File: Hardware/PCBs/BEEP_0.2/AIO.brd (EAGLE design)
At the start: 106.2 x 69.1 mm, 85 parts, among them IC1 ULN2803ASOP18, IC2 ULN2803ASOP18, IC3 74HC238SSOP, IC4 74HC238SSOP, IC5 TS34119SMD, U2 TB6612FNG, U3 ATXMEGA64D3-AU, X1 MICROMATCH-4, X10 MICROMATCH-10, X3 MICROMATCH-8, X4 MICROMATCH-8, X5 MICROMATCH-8, X8 MICROMATCH-8, X9 MICROMATCH-4

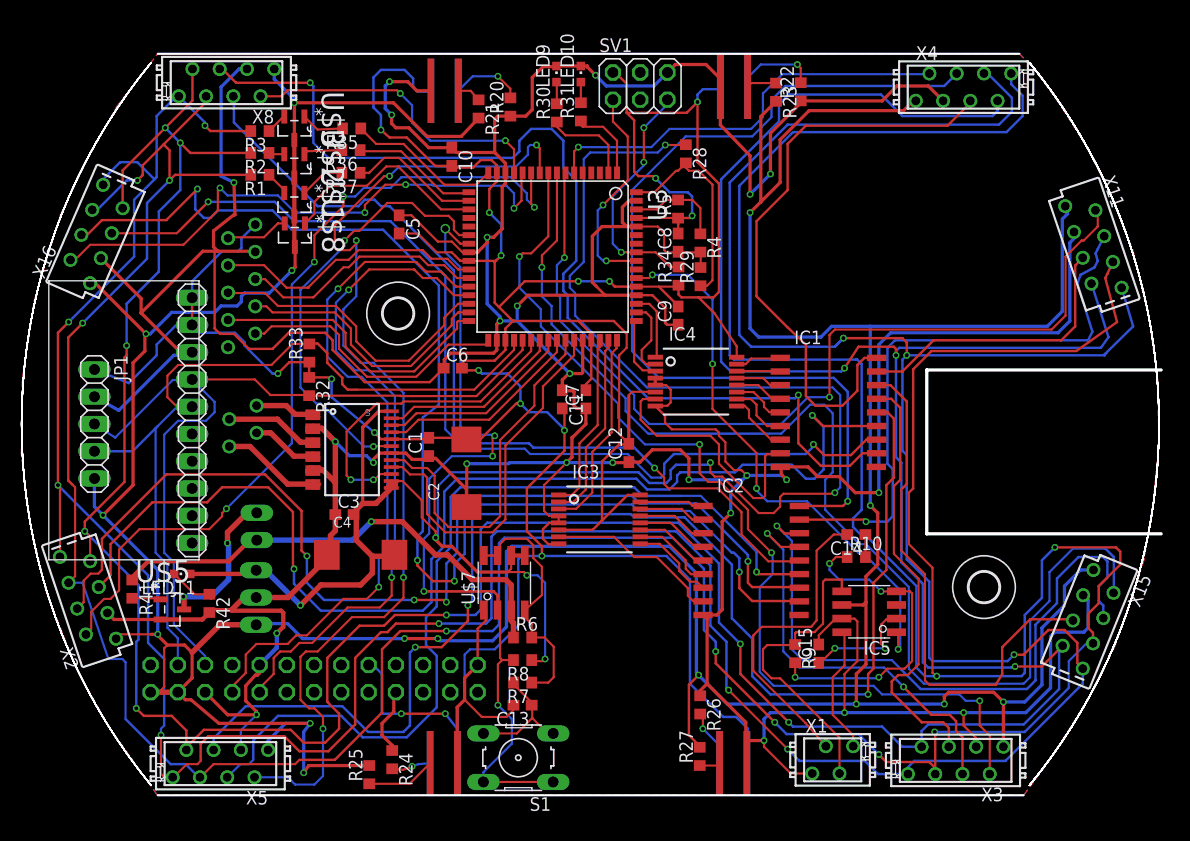
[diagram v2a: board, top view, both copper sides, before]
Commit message: rearrange connectors routing
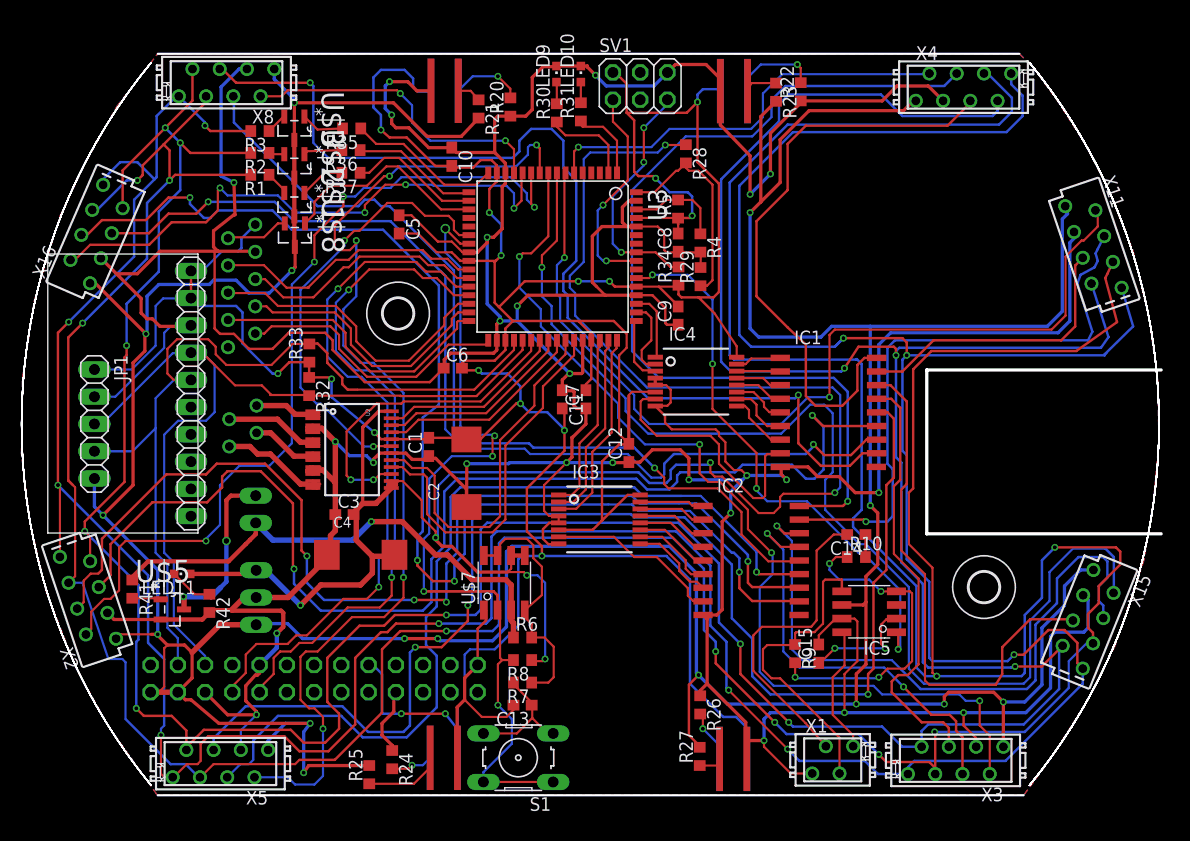
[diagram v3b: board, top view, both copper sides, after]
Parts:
- moved U$25 2.50 mm to (6.25, 43.1)
- moved JP13 1.60 mm to (18.6, 32.4)
- moved U$23 0.50 mm to (36.2, 12.2)
- moved U$22 0.40 mm to (63.2, 68.3)
- moved U$24 0.40 mm to (63.1, 12.1)
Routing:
- net SCL: track 78.5 -> 82.8 mm
- net SDA: track 77.5 -> 81.1 mm
- net +5V: track 397.0 -> 399.7 mm
- net LED_K5_OUT: track 106.6 -> 108.9 mm
- net BATT_GND: track 14.0 -> 16.3 mm
- net ADISTANCE_5: track 78.3 -> 80.5 mm
- net BATT_U: track 45.2 -> 47.1 mm
- net +3V3: track 368.6 -> 370.4 mm
- net IR_LED_K6_OUT: track 115.8 -> 114.1 mm
- net IR_LED_K5_OUT: track 98.0 -> 99.4 mm
- net N$20: track 6.48 -> 7.22 mm
- net GND: track 617.5 -> 618.2 mm

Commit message: move folders try to apply drc from sparkfun (wip) moved audio connetor add slice for camera flexcable
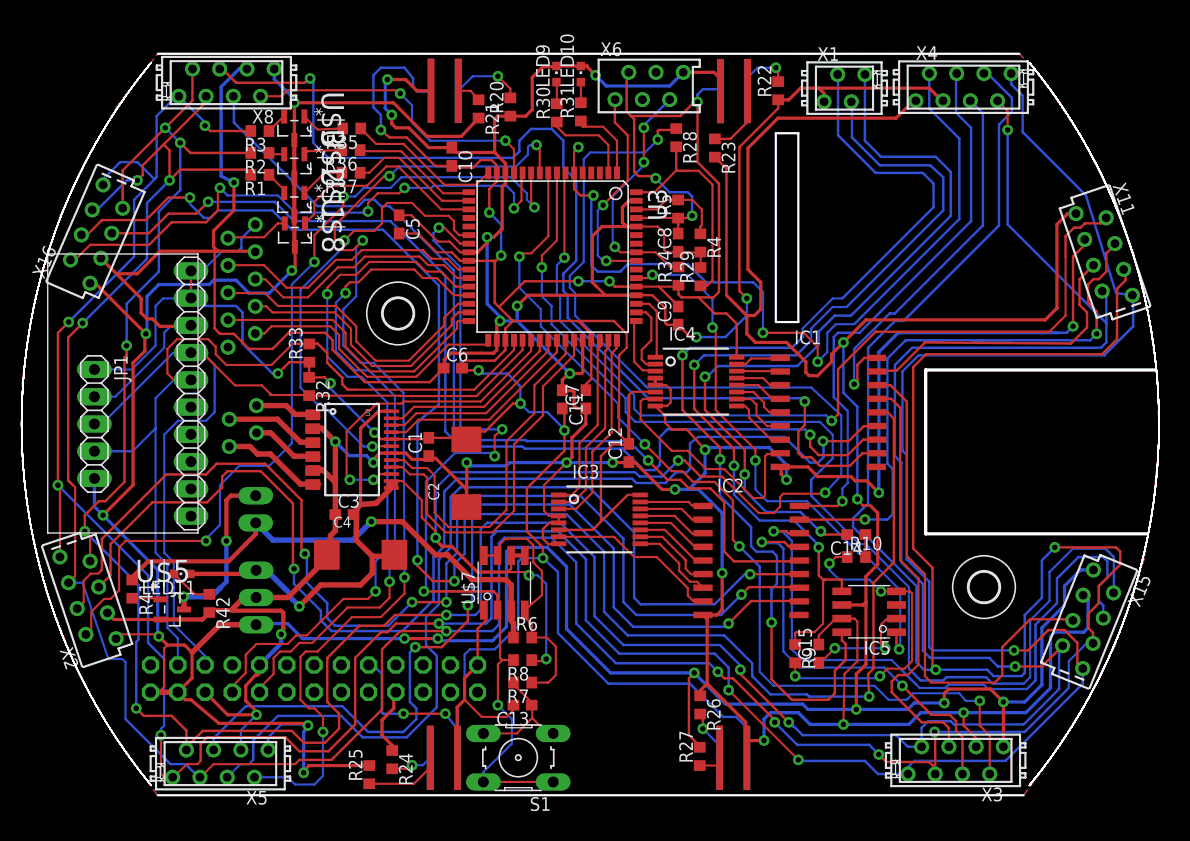
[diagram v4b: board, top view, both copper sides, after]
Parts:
- removed SV1: PDI, pinhead:2X03
- added X6: (no value), con-amp:FTOP-6
- moved X1 62.6 mm to (73.5, 71.6)
- moved R23 7.72 mm to (61.4, 66.0)
- moved R22 2.10 mm to (67.3, 71.4)
- moved R28 1.75 mm to (57.8, 67.0)
- moved X11 1.22 mm to (97.7, 56.1)
- moved U$24 0.10 mm to (63.1, 12.2)
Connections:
- net +3V3: now also X6.2; no longer SV1.2
- net AUDIO_IN: now also X1.1; no longer X1.3
- net GND: now also X6.6; no longer SV1.6
- net PDI_CLK: now also X6.5; no longer SV1.5
- net PDI_DATA: now also X6.1; no longer SV1.1
- net SPEAKER_O1: now also X1.3; no longer X1.1
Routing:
- net SPEAKER_O1: track 12.0 -> 96.4 mm, vias 0 -> 3
- net SPEAKER_O2: track 29.0 -> 84.2 mm, vias 0 -> 3
- net LED_A1_OUT: track 352.6 -> 307.1 mm, vias 11 -> 10
- net LED_A0_OUT: track 359.9 -> 314.7 mm, vias 10 -> 8
- net AUDIO_IN: track 29.5 -> 72.7 mm, vias 0 -> 3
- net ADISTANCE_0: track 39.4 -> 76.6 mm, vias 1 -> 4
- net IR_LED_K0_OUT: track 87.3 -> 51.9 mm
- net LED_A2_OUT: track 407.4 -> 377.9 mm
- net LED_K0_OUT: track 55.7 -> 36.8 mm, vias 0 -> 1
- net +5V: track 399.7 -> 411.7 mm
- net IR_LED_K5_OUT: track 99.4 -> 106.1 mm
- net GND: track 618.2 -> 623.2 mm, vias 25 -> 26
- net IR_LED_K4_OUT: track 83.2 -> 88.0 mm
- net IR_LED_K6_OUT: track 114.1 -> 117.7 mm
- net N$11: track 3.13 -> 6.59 mm
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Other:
- board size 106.2 x 69.1 mm -> 106 x 69.1 mm

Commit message: enhance routing, add external crystal, move components for Raspberry Pi
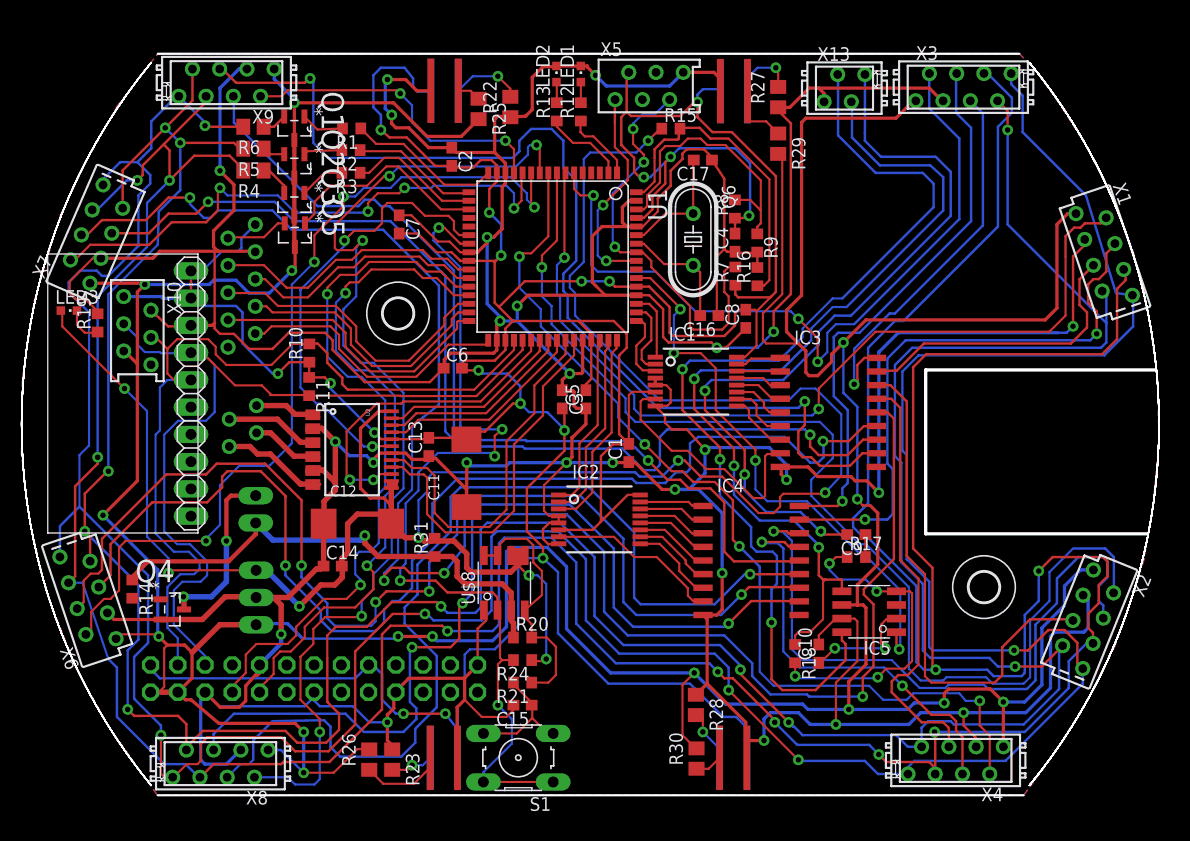
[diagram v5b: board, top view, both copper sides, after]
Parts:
- removed JP12: Step_Down_Conn, pinhead:1X03
- removed LED11: (no value), led:CHIPLED_0603
- removed R33, R42: (no value), rcl:R0603
- removed R34: 10K, rcl:R0603
- removed R35, R36, R37: 100R, rcl:R0603
- removed U$25: GY-81, BEEP:GY-81
- removed U$26: RASPBERRY-PI, BEEP:RASPERRRY-PI
- removed X15: (no value), con-amp:FSIDE-8
- added C16, C17: 22pF, rcl:C0603
- added LED3: blue, led:CHIPLED_0603
- added Q4, Q5: DMN2075U, BEEP:SOT95P240X112-3N
- added Q6: 32Mhz, crystal:HC49/S
- added R12: 220R, rcl:R0603
- added R13: 390R, rcl:R0603
- added R15, R16: (no value), rcl:R0603
- added R17: 3k, rcl:R0603
- added R18: 75k, rcl:R0603
- added R19: 1K, rcl:R0603
- added X12, X13: MICROMATCH-4, Con-amp-micromatch:MICROMATCH-4
- C10: value 100nF -> 1uF
- C11, C12: value 100nF -> 10uF; device rcl:C0603 -> rcl:SMC_D
- C13: value 1uF -> 100nF
- C2, C4: value 10uF -> 100nF; device rcl:SMC_D -> rcl:C0603
- IC1, IC2: value ULN2803ASOP18 -> 74HC238SSOP; device BEEP:SOP18 -> BEEP:SSOP16
- IC3, IC4: value 74HC238SSOP -> ULN2803ASOP18; device BEEP:SSOP16 -> BEEP:SOP18
- JP1: value (none) -> Step_Down_Conn; device pinhead:1X05 -> pinhead:1X03
- LED1: value (none) -> YELLOW
- LED2: value (none) -> RED
- R1, R2, R3: value (none) -> 100R
- R10: value 3k -> 10k
- R11, R20, R24: value (none) -> 10k
- R21: value (none) -> 100k
- R22, R23, R25, R26, R27, R28, R29, R30: device rcl:R0603 -> rcl:R0805
- R31: value (none) -> 0R
- R4, R5: value 10K -> (none); device rcl:R0603 -> rcl:R0805
- R6: value 10k -> (none); device rcl:R0603 -> rcl:R0805
- R7: value 100k -> 10K
- R8: value 10k -> (none)
- R9: value 75k -> (none)
- S1: value (none) -> On / Off
- U$5: value DMN2075U -> GY-81; device BEEP:SOT95P240X112-3N -> BEEP:GY-81
- U$7: value DMC3028LSD -> RASPBERRY-PI; device BEEP:SO08 -> BEEP:RASPERRRY-PI
- U$8: value DMN2075U -> DMC3028LSD; device BEEP:SOT95P240X112-3N -> BEEP:SO08
- X1: value MICROMATCH-4 -> Sens1; device Con-amp-micromatch:MICROMATCH-4 -> con-amp:FSIDE-8
- X10: value MICROMATCH-10 -> exp header; device Con-amp-micromatch:MICROMATCH-10 -> con-amp:FTOP-6
- X11: value (none) -> MICROMATCH-10; device con-amp:FSIDE-8 -> Con-amp-micromatch:MICROMATCH-10
- X2: value (none) -> Sens2
- X5: value MICROMATCH-8 -> PDI interface (ISP); device Con-amp-micromatch:MICROMATCH-8 -> con-amp:FTOP-6
- X6: value (none) -> Sens5; device con-amp:FTOP-6 -> con-amp:FSIDE-8
- X7: value (none) -> Sens6
- X9: value MICROMATCH-4 -> MICROMATCH-8; device Con-amp-micromatch:MICROMATCH-4 -> Con-amp-micromatch:MICROMATCH-8
- moved X2 93.2 mm to (96.2, 22.1), turned to 247.9 degrees
- moved X11 80.4 mm to (17.3, 53.2), flipped to the bottom, turned to 270 degrees
- moved X5 74.7 mm to (55.3, 71.8), turned to 0 degrees
- moved X6 70.8 mm to (3.00, 24.1), turned to 108.5 degrees
- moved U$7 65.7 mm to (91.4, 68.6), flipped to the bottom, turned to 270 degrees
- moved R23 64.4 mm to (31.4, 9.02)
- moved X8 63.5 mm to (15.3, 8.65)
- moved R25 62.9 mm to (39.4, 69.7), turned to 270 degrees
- moved X3 62.7 mm to (84.6, 71.7), turned to 0 degrees
- moved X4 62.7 mm to (83.9, 8.95), turned to 180 degrees
- moved R27 61.9 mm to (67.3, 70.8)
- moved R30 61.6 mm to (59.7, 9.12)
- moved C10 57.6 mm to (71.1, 18.9), turned to 90 degrees
- moved R10 54.4 mm to (23.6, 46.9), turned to 90 degrees
- moved R6 53.8 mm to (18.4, 68.0), turned to 180 degrees
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- renumbered JP13 to JP2, LED10 to LED1, LED9 to LED2, R32 to R11, R41 to R14, U$1 to Q3, U$2 to Q2, U$21 to U$9, U$22 to U$11, U$23 to U$10, U$24 to U$12, U$3 to Q1, U3 to U1, X16 to X7
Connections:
- new net N$14: C17.2, Q6.1, U1.59
- new net N$18: C16.2, Q6.2, U1.58
- net +3V3: now also C11.-, C13.2, C2.2, C3.2, C4.2, IC1.16, IC1.6, IC2.16, IC2.6, R10.1, R7.1, R8.1, U$5.3V3, U$5.VCC_IN, U$7.3V3@1, U$7.3V3@2, X10.1, X11.10, X5.2; no longer C10.2, C11.2, C12.2, C2.-, C9.2, IC3.16, IC3.6, IC4.16, IC4.6, JP1.1, R33.1, R34.1, R5.1, U$25.3V3, U$25.VCC_IN, U$26.3V3@1, U$26.3V3@2, X10.10, X6.2
- net +5V: now also JP1.3, Q5.D, R26.2, R29.2, R30.2, U$7.5V@1, U$7.5V@2, X1.1, X10.5, X6.1, X9.8; no longer JP1.5, JP12.3, R21.2, R23.2, R27.2, U$26.5V@1, U$26.5V@2, U$8.D, X11.1, X15.1, X5.8
- net +7V: now also C12.-, C14.2, JP1.1, LED3.A, R15.1, R24.1, R31.2, U$8.5, U$8.6; no longer C3.2, C4.-, JP12.1, LED11.A, R28.1, R8.1, U$7.5, U$7.6
- net ADISTANCE_0: now also X3.7; no longer X4.7
- net ADISTANCE_1: now also X1.2; no longer X11.2
- net ADISTANCE_2: now also X2.2; no longer X15.2
- net ADISTANCE_3: now also X4.7; no longer X3.7
- net ADISTANCE_4: now also X8.7; no longer X5.7
- net ADISTANCE_5: now also X6.2; no longer X2.2
- net ADISTANCE_7: now also X9.7; no longer X8.7
- net AUDIO_IN: now also C9.2, X13.1; no longer C14.2, X1.1
- net BATT_GND: now also Q4.D; no longer U$5.D
- net BATT_U: now also R20.1, R31.1, U$8.3; no longer R6.1, U$7.3
- net BATT_VOLTAGE: now also R15.2, R16.1; no longer R28.2, R29.1
- net BATT_WARN_0: now also R12.1; no longer R31.1
- net BATT_WARN_1: now also R13.1; no longer R30.1
- net COLOR_DIODE_1: now also X11.4; no longer X10.4
- net COLOR_DIODE_2: now also X11.3; no longer X10.3
- net COLOR_FREQ_OUT: now also X11.7; no longer X10.7
- net COLOR_SENSOR_1: now also X11.2; no longer X10.2
- net COLOR_SENSOR_2: now also X11.6; no longer X10.6
- net COLOR_SENSOR_3: now also X11.5; no longer X10.5
- net COLOR_SENSOR_PWM_LED: now also Q5.G; no longer U$8.G
- net ENCODER_L1: now also R22.2; no longer R20.2
- net ENCODER_L2: now also R27.2; no longer R22.2
- net ENCODER_R1: now also R23.2; no longer R24.2
- net ENCODER_R2: now also R28.2; no longer R26.2
- net GND: now also C10.2, C11.+, C12.+, C13.1, C14.1, C16.1, C17.1, C2.1, C4.1, IC1.4, IC1.5, IC1.8, IC2.4, IC2.5, IC2.8, IC3.9, IC4.9, Q4.S, R16.2, R19.2, R23.1, R27.1, R28.1, R9.2, U$5.GND, U$7.GND@1, U$7.GND@2, U$7.GND@3, U$7.GND@4, U$7.GND@5, U$8.1, X1.3, X10.2, X11.8, X13.4, X6.3, X9.6; no longer C10.1, C11.1, C12.1, C13.2, C2.+, C4.+, C9.1, IC1.9, IC2.9, IC3.4, IC3.5, IC3.8, IC4.4, IC4.5, IC4.8, JP12.2, R20.1, R24.1, R26.1, R29.2, R4.2, R42.2, U$25.GND, U$26.GND@1, U$26.GND@2, U$26.GND@3, U$26.GND@4, U$26.GND@5, U$5.S, U$7.1, X1.4, X10.8, X11.3, X15.3, X6.6
- net IR_LED_K0: now also IC2.15, IC4.1; no longer IC2.1, IC3.15
- net IR_LED_K0_OUT: now also IC4.18, X3.5; no longer IC2.18, X4.5
- net IR_LED_K1: now also IC2.14, IC4.2; no longer IC2.2, IC3.14
- net IR_LED_K1_OUT: now also IC4.17, X1.4; no longer IC2.17, X11.4
- net IR_LED_K2_OUT: now also IC4.16, X2.4; no longer IC2.16, X15.4
- net IR_LED_K3_OUT: now also IC4.15, X4.5; no longer IC2.15, X3.5
- net IR_LED_K4_OUT: now also IC4.13, X8.5; no longer IC2.13, X5.5
- net IR_LED_K5_OUT: now also IC4.12, X6.4; no longer IC2.12, X2.4
- net IR_LED_K6_OUT: now also IC4.11; no longer IC2.11
- net IR_LED_K7_OUT: now also IC4.14, X9.5; no longer IC2.14, X8.5
- net IR_LED_MK0: now also IC2.1; no longer IC3.1
- net IR_LED_MK1: now also IC2.2; no longer IC3.2
- net IR_LED_MK2: now also IC2.3; no longer IC3.3
- net LED_A0: now also R1.1; no longer R35.1
- net LED_A0_OUT: now also R6.2, X1.8, X6.8, X9.1; no longer R3.2, X11.8, X15.8, X5.1
- net LED_A1: now also R2.1; no longer R36.1
- net LED_A1_OUT: now also R5.2, X1.7, X6.7, X9.2; no longer R2.2, X11.7, X15.7, X5.2
- net LED_A2: now also R3.1; no longer R37.1
- net LED_A2_OUT: now also R4.2, X1.6, X6.6, X9.3; no longer R1.2, X11.6, X15.6, X5.3
- net LED_K0_OUT: now also IC3.18, X3.4; no longer IC1.18, X4.4
- net LED_K1_OUT: now also IC3.17, X1.5; no longer IC1.17, X11.5
- net LED_K2_OUT: now also IC3.16, X2.5; no longer IC1.16, X15.5
- net LED_K3_OUT: now also IC3.15, X4.4; no longer IC1.15, X3.4
- net LED_K4_OUT: now also IC3.14, X8.4; no longer IC1.14, X5.4
- net LED_K5_OUT: now also IC3.13, X6.5; no longer IC1.13, X2.5
- net LED_K6_OUT: now also IC3.12; no longer IC1.12
- net LED_K7_OUT: now also IC3.11, X9.4; no longer IC1.11, X8.4
- net MOTOR_A_OUT1: now also X12.1; no longer X9.1
- net MOTOR_A_OUT2: now also X12.2; no longer X9.2
- net MOTOR_B_OUT1: now also X12.4; no longer X9.4
- net MOTOR_B_OUT2: now also X12.3; no longer X9.3
- net N$1: now also R4.1; no longer R1.1
- net N$10: now also IC2.10, IC4.6; no longer IC2.6, IC3.10
- net N$11: now also R29.1; no longer R23.1
- net N$12: now also IC2.9, IC4.7; no longer IC2.7, IC3.9
- net N$13: now also IC2.7, IC4.8; no longer IC2.8, IC3.7
- net N$15: now also R17.1, R18.2; no longer R10.1, R9.2
- net N$16: now also C15.1, R21.2; no longer C13.1, R7.2
- net N$17: now also C9.1, R17.2; no longer C14.1, R10.2
- net N$19: now also LED3.C, R19.1; no longer LED11.C, R42.1
- net N$2: now also R5.1; no longer R2.1
- net N$20: now also R26.1; no longer R25.1
- net N$21: now also IC1.15, IC3.1; no longer IC1.1, IC4.15
- net N$22: now also R20.2, R21.1, U$8.4, U$8.7, U$8.8; no longer R6.2, R7.1, U$7.4, U$7.7, U$7.8
- net N$23: now also R25.1; no longer R21.1
- net N$24: now also IC1.14, IC3.2; no longer IC1.2, IC4.14
- net N$26: now also R30.1; no longer R27.1
- net N$27: now also IC1.13, IC3.3; no longer IC1.3, IC4.13
- net N$28: now also IC1.12, IC3.4; no longer IC1.4, IC4.12
- net N$29: now also R13.2; no longer R30.2
- net N$3: now also R6.1; no longer R3.1
- net N$30: now also IC1.11, IC3.5; no longer IC1.5, IC4.11
- net N$31: now also IC1.10, IC3.6; no longer IC1.6, IC4.10
- net N$32: now also R12.2; no longer R31.2
- net N$33: now also IC1.9, IC3.7; no longer IC1.7, IC4.9
- net N$34: now also IC1.7, IC3.8; no longer IC1.8, IC4.7
- net N$36: now also C10.1; no longer C15.1
- net N$38: now also R1.2; no longer R35.2
- net N$39: now also R2.2; no longer R36.2
- net N$4: now also R8.2, R9.1; no longer R4.1, R5.2
- net N$40: now also R3.2; no longer R37.2
- net N$5: now also Q5.S, X11.9; no longer U$8.S, X10.9
- net N$6: now also IC2.13, IC4.3; no longer IC2.3, IC3.13
- net N$7: now also IC2.12, IC4.4; no longer IC2.4, IC3.12
- net N$8: now also Q4.G; no longer U$5.G
- net N$9: now also IC2.11, IC4.5; no longer IC2.5, IC3.11
- net PDI_CLK: now also R7.2, X5.5; no longer R34.2, X6.5
- net PDI_DATA: now also X5.1; no longer X6.1
- net POWER_OFF: now also R24.2, U$8.2; no longer R8.2, U$7.2
- net RGB_LED_MK0: now also IC1.1; no longer IC4.1
- net RGB_LED_MK1: now also IC1.2; no longer IC4.2
- net RGB_LED_MK2: now also IC1.3; no longer IC4.3
- net RPI_RX: now also U$7.GPIO_15; no longer U$26.GPIO_15
- net RPI_TX: now also U$7.GPIO_14; no longer U$26.GPIO_14
- net SCL: now also U$5.SCL, U$7.GPIO_1, X10.3; no longer JP1.3, U$25.SCL, U$26.GPIO_1
- net SDA: now also R10.2, U$5.SDA, U$7.GPIO_0, X10.4; no longer JP1.4, R33.2, U$25.SDA, U$26.GPIO_0
- net SPEAKER_O1: now also X13.3; no longer X1.3
- net SPEAKER_O2: now also R18.1, X13.2; no longer R9.1, X1.2
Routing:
- net GND: track 623.2 -> 673.1 mm
- net +3V3: track 369.3 -> 409.1 mm, vias 17 -> 18
- net +7V: track 185.5 -> 216.0 mm, vias 7 -> 9
- net N$4: track 9.16 -> 26.3 mm
- net PDI_CLK: track 22.7 -> 39.2 mm
- net N$14: track 0.00 -> 11.1 mm
- net N$18: track 0.00 -> 11.1 mm
- net BATT_VOLTAGE: track 20.9 -> 29.8 mm
- net ADISTANCE_0: track 76.6 -> 70.7 mm, vias 4 -> 3
- net +5V: track 411.7 -> 406.1 mm
- net IR_LED_K6_OUT: track 117.7 -> 122.4 mm
- net IR_LED_K4_OUT: track 88.0 -> 92.7 mm
- net POWER_OFF: track 82.0 -> 85.3 mm
- net LED_A2_OUT: track 377.9 -> 374.9 mm
- net SPEAKER_O1: track 96.4 -> 93.7 mm
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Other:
- outline, holes or cut-outs redrawn

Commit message: Use PORTC for TWI, bcause of really annoying errata that states that TWI on PORT E is unusable for Revisions prior of I. damn errata!!!
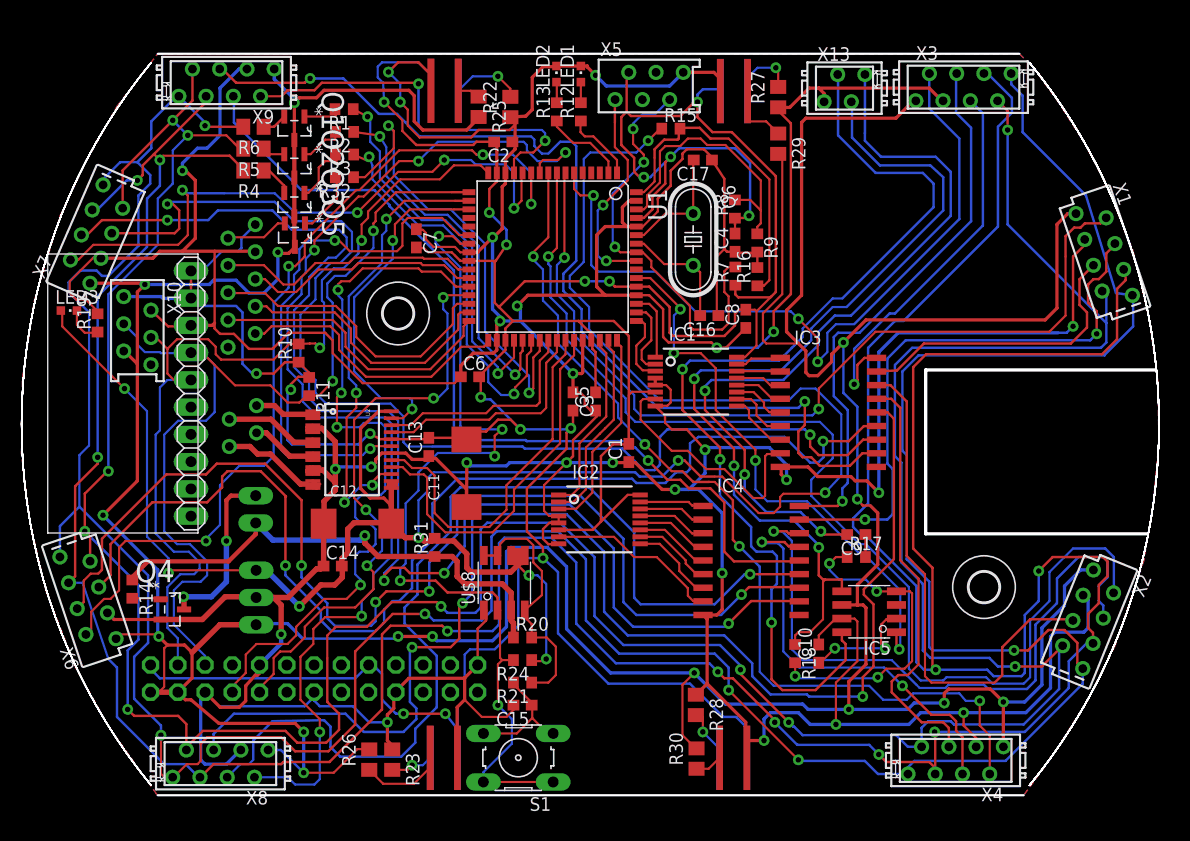
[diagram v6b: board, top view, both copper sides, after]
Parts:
- added R32: 100R, rcl:R0603
- moved C2 5.00 mm to (41.7, 66.6), turned to 180 degrees
- moved C7 2.06 mm to (33.6, 57.6)
- moved R1 1.93 mm to (26.9, 69.6)
- moved R2 1.80 mm to (26.9, 67.5)
- moved R3 1.80 mm to (26.9, 65.4)
- moved C6 1.79 mm to (38.6, 44.7)
- moved C3 1.02 mm to (48.2, 42.4)
- moved R10 1.00 mm to (22.6, 46.9)
- moved C5 0.92 mm to (50.3, 42.4)
- moved R25 0.20 mm to (39.4, 69.9)
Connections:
- new net N$25: Q5.G, R32.2
- net COLOR_SENSOR_PWM_LED: now also R32.1, U1.39; no longer Q5.G, U1.19
- net LED_A0: now also U1.36; no longer U1.16
- net LED_A1: now also U1.37; no longer U1.17
- net LED_A2: now also U1.38; no longer U1.18
- net MOTOR_A_PWM: now also U1.19; no longer U1.39
- net MOTOR_B_PWM: now also U1.18; no longer U1.38
- net SCL: now also U1.17; no longer U1.37
- net SDA: now also U1.16; no longer U1.36
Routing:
- net LED_A2: track 12.5 -> 37.3 mm, vias 0 -> 2
- net COLOR_SENSOR_PWM_LED: track 19.8 -> 44.0 mm, vias 0 -> 2
- net LED_A1: track 11.8 -> 34.5 mm, vias 0 -> 2
- net LED_A0: track 14.5 -> 35.5 mm, vias 0 -> 2
- net MOTOR_A_PWM: track 17.4 -> 32.4 mm, vias 0 -> 2
- net MOTOR_B_PWM: track 30.0 -> 42.6 mm, vias 2 -> 4
- net LED_K6_OUT: track 96.7 -> 108.1 mm
- net MOTOR_STBY: track 41.7 -> 50.4 mm
- net SCL: track 83.2 -> 91.6 mm, vias 0 -> 2
- net ADISTANCE_7: track 29.3 -> 36.9 mm
- net RPI_RX: track 62.4 -> 55.0 mm, vias 2 -> 4
- net ADISTANCE_4: track 97.4 -> 104.0 mm
- net N$25: track 0.00 -> 5.95 mm
- net SDA: track 80.9 -> 86.0 mm, vias 0 -> 2
- net ADISTANCE_6: track 53.2 -> 57.7 mm
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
